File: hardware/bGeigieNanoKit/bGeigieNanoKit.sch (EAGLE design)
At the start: 35 parts, among them T1 2SC1815

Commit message: cleaning up libs and updating brd
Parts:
- U$3: device open_hw_sockets:ULTIMATE_GPS -> open_hw_sockets:ULTIMATE_GPSTOP
- U$4: device open_hw_sockets:SSD1306_128X32_SPI_LCD -> open_hw_sockets:SSD1306_128X32_SPI_LCDTOP
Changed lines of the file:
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@@
 <setting verticaltext="up"/>
 </settings>
-<grid distance="0.1" unitdist="inch" unit="inch" style="dots" multiple="1" display="yes" altdistance="0.01" altunitdist="inch" altunit="inch"/>
+<grid distance="0.1" unitdist="inch" unit="inch" style="lines" multiple="1" display="no" altdistance="0.01" altunitdist="inch" altunit="inch"/>
 <layers>
-<layer number="1" name="Top" color="4" fill="1" visible="no" active="no"/>
-<layer number="2" name="Route2" color="1" fill="3" visible="no" active="no"/>
-<layer number="3" name="Route3" color="4" fill="3" visible="no" active="no"/>
-<layer number="14" name="Route14" color="1" fill="6" visible="no" active="no"/>
-<layer number="15" name="Route15" color="4" fill="6" visible="no" active="no"/>
-<layer number="16" name="Bottom" color="1" fill="1" visible="no" active="no"/>
-<layer number="17" name="Pads" color="2" fill="1" visible="no" active="no"/>
-<layer number="18" name="Vias" color="2" fill="1" visible="no" active="no"/>
-<layer number="19" name="Unrouted" color="6" fill="1" visible="no" active="no"/>
-<layer number="20" name="Dimension" color="15" fill="1" visible="no" active="no"/>
-<layer number="21" name="tPlace" color="14" fill="1" visible="no" active="no"/>
-<layer number="22" name="bPlace" color="13" fill="1" visible="no" active="no"/>
-<layer number="23" name="tOrigins" color="15" fill="1" visible="no" active="no"/>
-<layer number="24" name="bOrigins" color="15" fill="1" visible="no" active="no"/>
-<layer number="25" name="tNames" color="7" fill="1" visible="no" active="no"/>
-<layer number="26" name="bNames" color="7" fill="1" visible="no" active="no"/>
-<layer number="27" name="tValues" color="7" fill="1" visible="no" active="no"/>
-<layer number="28" name="bValues" color="7" fill="1" visible="no" active="no"/>
+<layer number="1" name="Top" color="4" fill="1" visible="yes" active="no"/>
+<layer number="2" name="Route2" color="1" fill="3" visible="yes" active="no"/>
+<layer number="3" name="Route3" color="4" fill="3" visible="yes" active="no"/>
+<layer number="14" name="Route14" color="1" fill="6" visible="yes" active="no"/>
+<layer number="15" name="Route15" color="4" fill="6" visible="yes" active="no"/>
+<layer number="16" name="Bottom" color="1" fill="1" visible="yes" active="no"/>
+<layer number="17" name="Pads" color="2" fill="1" visible="yes" active="no"/>
+<layer number="18" name="Vias" color="2" fill="1" visible="yes" active="no"/>
+<layer number="19" name="Unrouted" color="6" fill="1" visible="yes" active="no"/>
+<layer number="20" name="Dimension" color="15" fill="1" visible="yes" active="no"/>
+<layer number="21" name="tPlace" color="14" fill="1" visible="yes" active="no"/>
+<layer number="22" name="bPlace" color="13" fill="1" visible="yes" active="no"/>
+<layer number="23" name="tOrigins" color="15" fill="1" visible="yes" active="no"/>
+<layer number="24" name="bOrigins" color="15" fill="1" visible="yes" active="no"/>
+<layer number="25" name="tNames" color="7" fill="1" visible="yes" active="no"/>
+<layer number="26" name="bNames" color="7" fill="1" visible="yes" active="no"/>
+<layer number="27" name="tValues" color="7" fill="1" visible="yes" active="no"/>
+<layer number="28" name="bValues" color="7" fill="1" visible="yes" active="no"/>
 <layer number="29" name="tStop" color="7" fill="3" visible="no" active="no"/>
 <layer number="30" name="bStop" color="7" fill="6" visible="no" active="no"/>
@@
 <layer number="35" name="tGlue" color="7" fill="4" visible="no" active="no"/>
 <layer number="36" name="bGlue" color="7" fill="5" visible="no" active="no"/>
-<layer number="37" name="tTest" color="7" fill="1" visible="no" active="no"/>
-<layer number="38" name="bTest" color="7" fill="1" visible="no" active="no"/>
+<layer number="37" name="tTest" color="7" fill="1" visible="yes" active="no"/>
+<layer number="38" name="bTest" color="7" fill="1" visible="yes" active="no"/>
 <layer number="39" name="tKeepout" color="4" fill="11" visible="no" active="no"/>
 <layer number="40" name="bKeepout" color="1" fill="11" visible="no" active="no"/>
@@
 <layer number="44" name="Drills" color="7" fill="1" visible="no" active="no"/>
 <layer number="45" name="Holes" color="7" fill="1" visible="no" active="no"/>
-<layer number="46" name="Milling" color="3" fill="1" visible="no" active="no"/>
-<layer number="47" name="Measures" color="7" fill="1" visible="no" active="no"/>
-<layer number="48" name="Document" color="7" fill="1" visible="no" active="no"/>
-<layer number="49" name="Reference" color="7" fill="1" visible="no" active="no"/>
-<layer number="50" name="dxf" color="7" fill="1" visible="no" active="no"/>
-<layer number="51" name="tDocu" color="7" fill="1" visible="no" active="no"/>
-<layer number="52" name="bDocu" color="7" fill="1" visible="no" active="no"/>
-<layer number="53" name="tGND_GNDA" color="7" fill="9" visible="no" active="no"/>
-<layer number="54" name="bGND_GNDA" color="1" fill="9" visible="no" active="no"/>
-<layer number="56" name="wert" color="7" fill="1" visible="no" active="no"/>
+<layer number="46" name="Milling" color="3" fill="1" visible="yes" active="no"/>
+<layer number="47" name="Measures" color="7" fill="1" visible="yes" active="no"/>
+<layer number="48" name="Document" color="7" fill="1" visible="yes" active="no"/>
+<layer number="49" name="Reference" color="7" fill="1" visible="yes" active="no"/>
+<layer number="50" name="dxf" color="7" fill="1" visible="yes" active="no"/>
+<layer number="51" name="tDocu" color="7" fill="1" visible="yes" active="no"/>
+<layer number="52" name="bDocu" color="7" fill="1" visible="yes" active="no"/>
+<layer number="53" name="tGND_GNDA" color="7" fill="9" visible="yes" active="no"/>
+<layer number="54" name="bGND_GNDA" color="1" fill="9" visible="yes" active="no"/>
+<layer number="56" name="wert" color="7" fill="1" visible="yes" active="no"/>
 <layer number="91" name="Nets" color="2" fill="1" visible="yes" active="yes"/>
 <layer number="92" name="Busses" color="1" fill="1" visible="yes" active="yes"/>
@@
 <parts>
 <part name="FRAME1" library="frames" deviceset="FRAME_A_L" device=""/>
-<part name="U$4" library="open_hw_sockets" deviceset="SSD1306_128X32_SPI_LCD" device="" value="LCD"/>
-<part name="U$3" library="open_hw_sockets" deviceset="ULTIMATE_GPS" device="" value="GPS"/>
+<part name="U$4" library="open_hw_sockets" deviceset="SSD1306_128X32_SPI_LCD" device="TOP" value="LCD"/>
+<part name="U$3" library="open_hw_sockets" deviceset="ULTIMATE_GPS" device="TOP" value="GPS"/>
 <part name="LED1" library="adafruit" deviceset="LED" device="3MM"/>
 <part name="LED2" library="adafruit" deviceset="LED" device="3MM" value="RED"/>

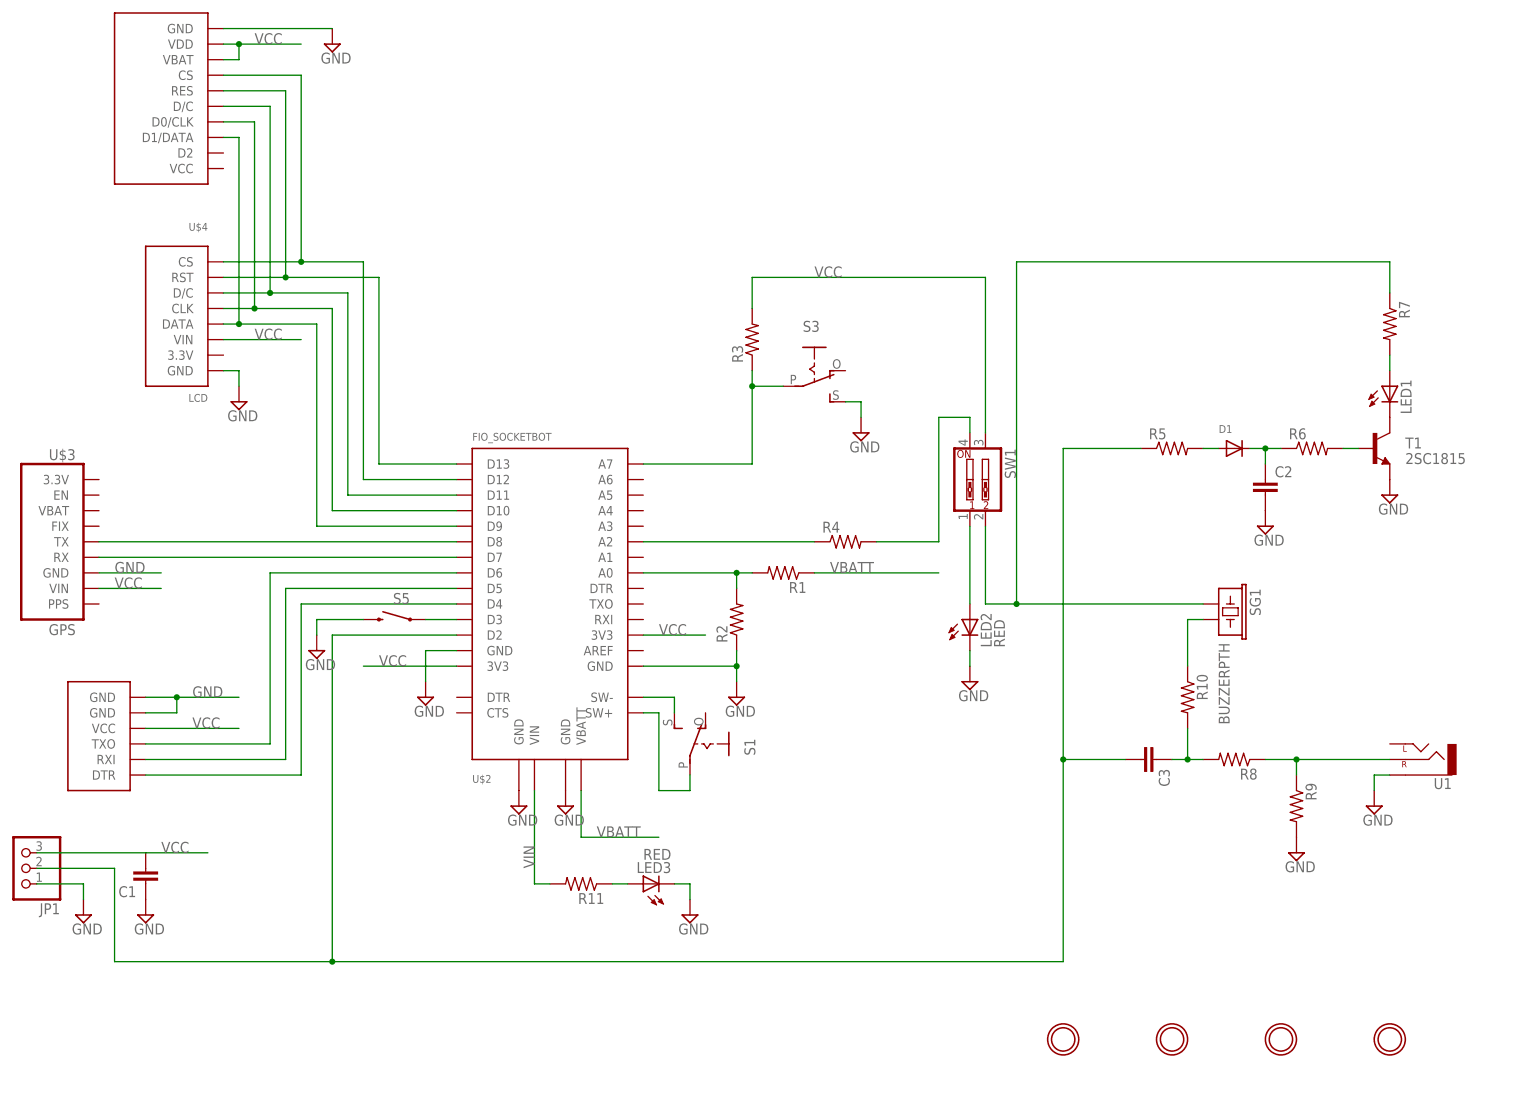
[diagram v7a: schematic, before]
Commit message: smashing all parts and moving labels to be visable adding current limit resistor for charge led add lables to leds
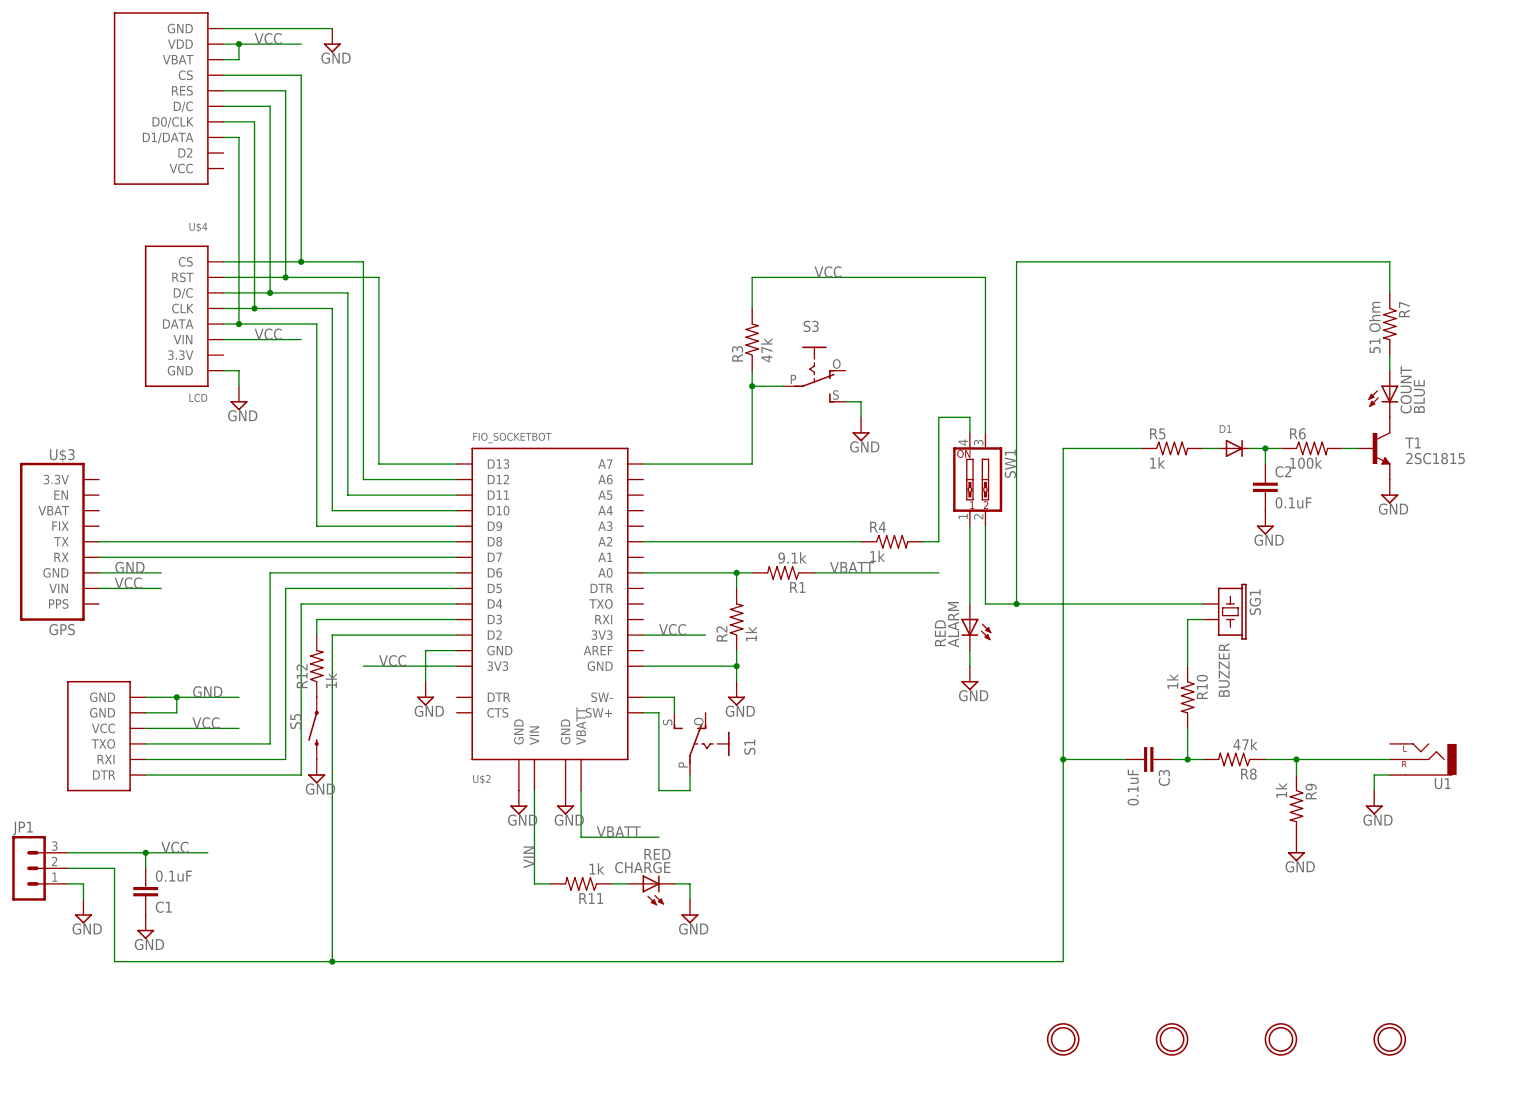
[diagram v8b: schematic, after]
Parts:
- added R12: 1k, rcl:R-US_0207/10
- C1, C2, C3: value (none) -> 0.1uF
- COUNT: value (none) -> BLUE
- JP1: device microbuilder:HEADER-1X376MIL -> con-lstb:MA03-1
- R1: value (none) -> 9.1k
- R10, R11, R2, R4, R5, R9: value (none) -> 1k
- R3, R8: value (none) -> 47k
- R6: value (none) -> 100k
- R7: value (none) -> 51 Ohm
- SG1: value BUZZERPTH -> BUZZER
- U$1: value OPENLOG_MIN -> OPENLOG_MINITOP; device open_hw_sockets:OPENLOG_MIN -> open_hw_sockets:OPENLOG_MINITOP
- renumbered LED1 to COUNT, LED2 to ALARM, LED3 to CHARGE
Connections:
- new net N$30: R12.2, U$2.D3
- net N$20: now also R12.1; no longer U$2.D3
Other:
- moved on the sheet: C1, R4, S5
